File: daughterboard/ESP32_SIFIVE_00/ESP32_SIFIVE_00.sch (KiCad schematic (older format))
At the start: 2 parts, among them J1 m2_keyA_67pin_daughterboard

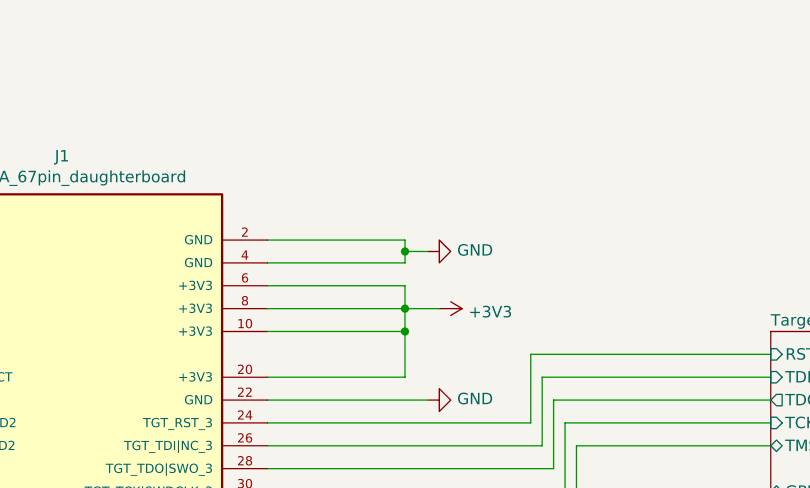
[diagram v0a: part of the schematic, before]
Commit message: ERC on daughterboards
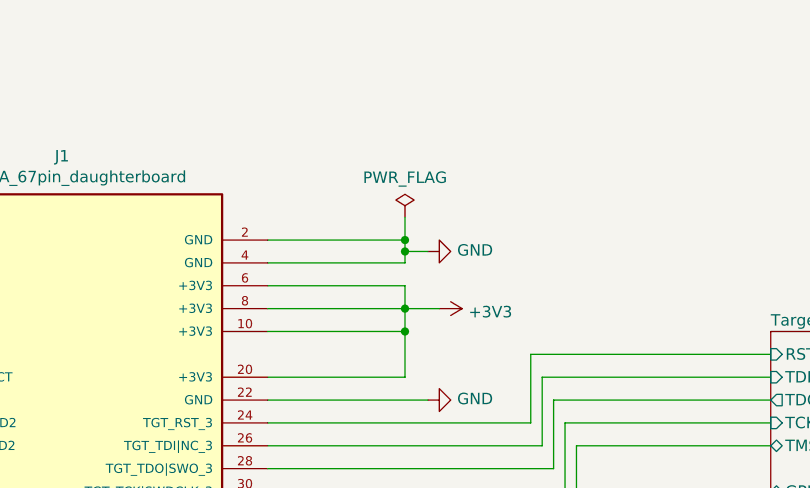
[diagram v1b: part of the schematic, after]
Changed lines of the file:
@@
 	0    -1   -1   0
 $EndComp
+$Comp
+L power:PWR_FLAG #FLG0103
+U 1 1 619024C3
+P 7500 1500
+F 0 "#FLG0103" H 7500 1575 50  0001 C CNN
+F 1 "PWR_FLAG" H 7500 1673 50  0000 C CNN
+F 2 "" H 7500 1500 50  0001 C CNN
+F 3 "~" H 7500 1500 50  0001 C CNN
+	1    7500 1500
+	1    0    0    -1
+$EndComp
+Wire Wire Line
+	7500 1500 7500 1600
+Connection ~ 7500 1600
 $EndSCHEMATC
